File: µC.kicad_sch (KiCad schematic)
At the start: 18 parts, among them J1 Conn_01x02_Pin, J4 USB_C_Receptacle_USB2.0_14P, Q1 NPN, Q2 NPN, Q3 NPN, SW4 SW_Push, U2 ESP32-S3-WROOM-1

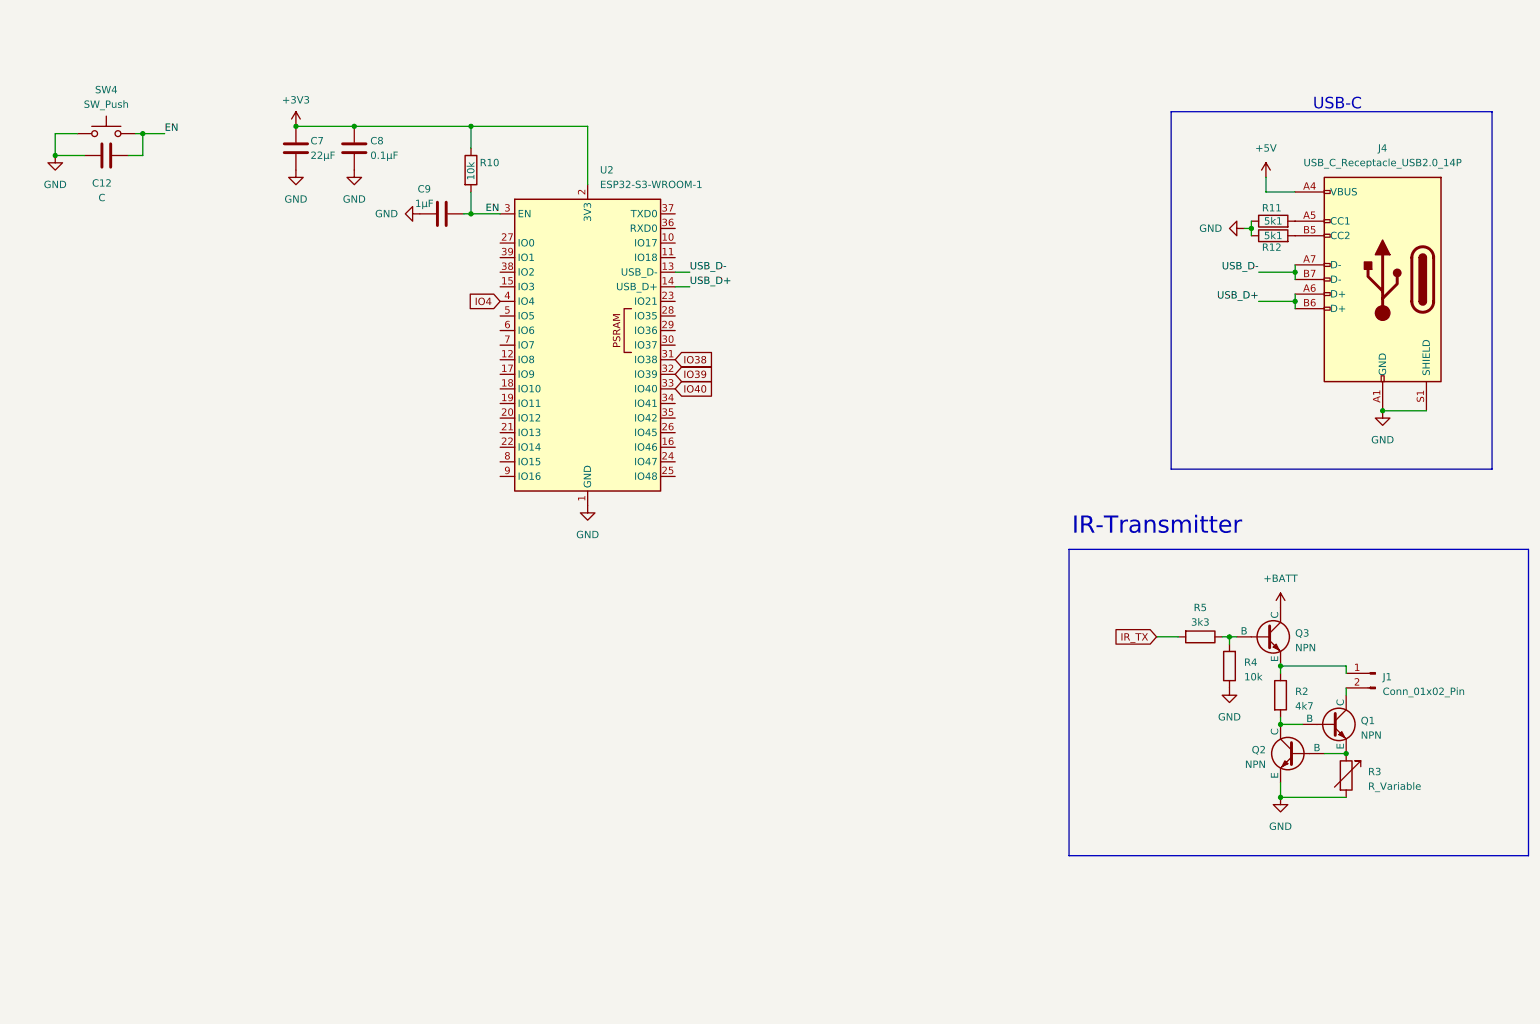
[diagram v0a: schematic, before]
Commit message: simulated IR-constant-current circuit, worked on schematic
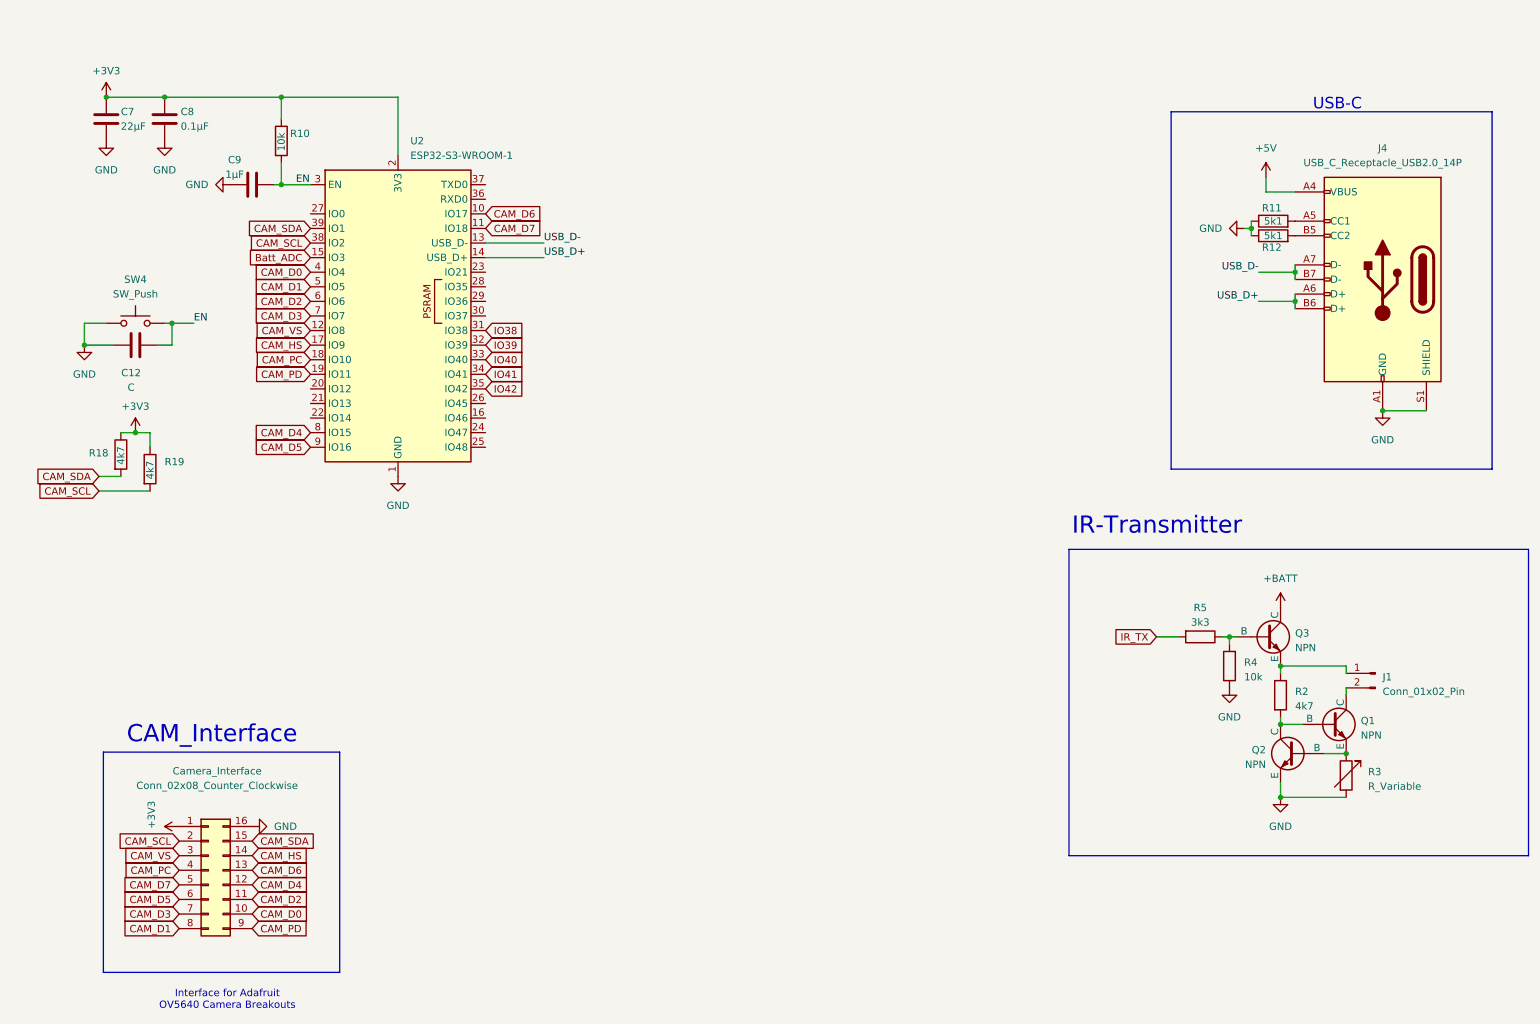
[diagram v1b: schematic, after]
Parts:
- added Camera_Interface: Conn_02x08_Counter_Clockwise, symbol Connector_Generic:Conn_02x08_Counter_Clockwise
- added R18, R19: 4k7, symbol Device:R
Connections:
- net +3V3: now also Camera_Interface.1 (Pin_1), R18.1, R19.1
- net GND: now also Camera_Interface.16 (Pin_16)
- net CAM_D6: now reaches U2.10 (IO17)
- net CAM_D6: now also Camera_Interface.13 (Pin_13)
- net CAM_D7: now reaches U2.11 (IO18)
- net CAM_D7: now also Camera_Interface.5 (Pin_5)
- net CAM_VS: now reaches U2.12 (IO8)
- net CAM_VS: now also Camera_Interface.3 (Pin_3)
- net Batt_ADC: now reaches U2.15 (IO3)
- net CAM_HS: now reaches U2.17 (IO9)
- net CAM_HS: now also Camera_Interface.14 (Pin_14)
- net CAM_PC: now reaches U2.18 (IO10)
- net CAM_PC: now also Camera_Interface.4 (Pin_4)
- net CAM_PD: now reaches U2.19 (IO11)
- net CAM_PD: now also Camera_Interface.9 (Pin_9)
- net IO41: now reaches U2.34 (IO41)
- net IO42: now reaches U2.35 (IO42)
- net CAM_SCL: now reaches U2.38 (IO2)
- net CAM_SCL: now also Camera_Interface.2 (Pin_2), R19.2
- net CAM_SDA: now reaches U2.39 (IO1)
- net CAM_SDA: now also Camera_Interface.15 (Pin_15), R18.2
- net CAM_D1: now reaches U2.5 (IO5)
- net CAM_D1: now also Camera_Interface.8 (Pin_8)
- net CAM_D2: now reaches U2.6 (IO6)
- net CAM_D2: now also Camera_Interface.11 (Pin_11)
- net CAM_D3: now reaches U2.7 (IO7)
- net CAM_D3: now also Camera_Interface.7 (Pin_7)
- net CAM_D4: now reaches U2.8 (IO15)
- net CAM_D4: now also Camera_Interface.12 (Pin_12)
- net CAM_D5: now reaches U2.9 (IO16)
- net CAM_D5: now also Camera_Interface.6 (Pin_6)
- net IO4 renamed CAM_D0
- net CAM_D0: now also Camera_Interface.10 (Pin_10)
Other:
- note added: "CAM_Interface"
- note added: "Interface for Adafruit OV5640 Camera Breakouts"
- moved on the sheet: C12, C7, C8, C9, R10, SW4, U2

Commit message: prepared for jlcpcb ordering.
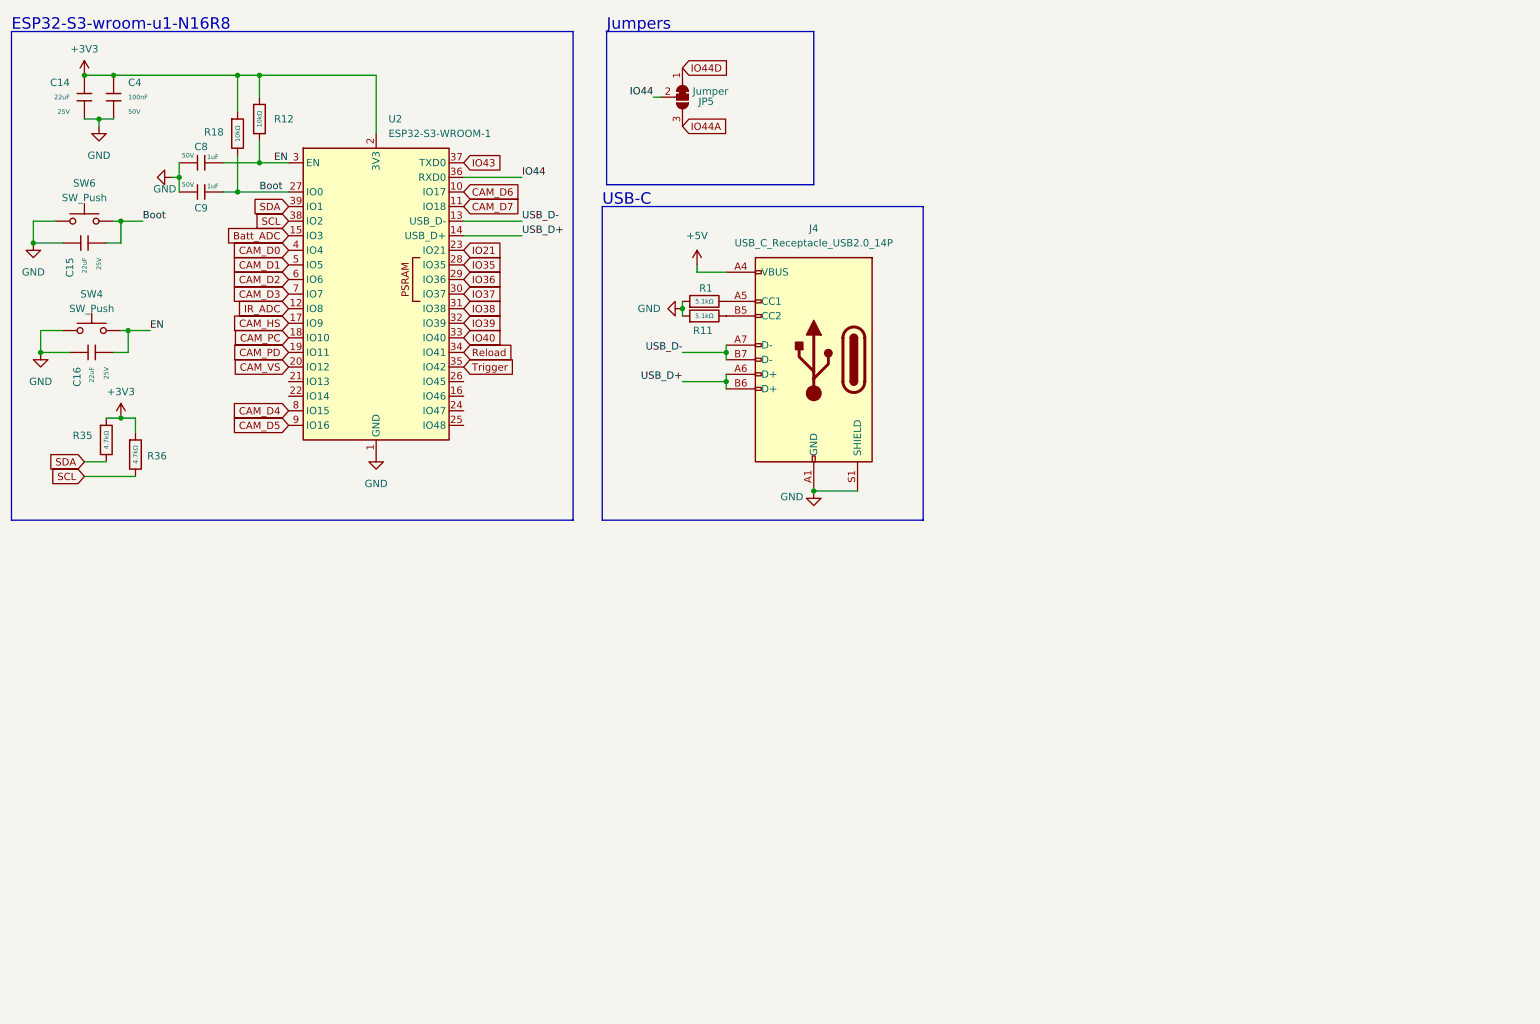
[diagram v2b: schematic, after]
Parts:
- removed C12: C, symbol Device:C
- removed C7: 22µF, symbol Device:C
- removed C8: 0.1µF, symbol Device:C
- removed C9: 1µF, symbol Device:C
- removed Camera_Interface: Conn_02x08_Counter_Clockwise, symbol Connector_Generic:Conn_02x08_Counter_Clockwise
- removed J1: Conn_01x02_Pin, symbol Connector:Conn_01x02_Pin
- removed Q1, Q2, Q3: NPN, symbol Simulation_SPICE:NPN
- removed R10, R4: 10k, symbol Device:R
- removed R11, R12: 5k1, symbol Device:R
- removed R18, R19, R2: 4k7, symbol Device:R
- removed R3: R_Variable, symbol Device:R_Variable
- removed R5: 3k3, symbol Device:R
- added C14, C15, C16: 22uF, PCM_JLCPCB:C_0805, symbol PCM_JLCPCB-Capacitors:0805,22uF
- added C4: 100nF, PCM_JLCPCB:C_0603, symbol PCM_JLCPCB-Capacitors:0603,100nF
- added C8, C9: 1uF, PCM_JLCPCB:C_0603, symbol PCM_JLCPCB-Capacitors:0603,1uF
- added JP5: Jumper, symbol Jumper:SolderJumper_3_Bridged12
- added R1, R11: 5.1kΩ, PCM_JLCPCB:R_0603, symbol PCM_JLCPCB-Resistors:0603,5.1kΩ
- added R12, R18: 10kΩ, PCM_JLCPCB:R_0603, symbol PCM_JLCPCB-Resistors:0603,10kΩ
- added R35, R36: 4.7kΩ, PCM_JLCPCB:R_0603, symbol PCM_JLCPCB-Resistors:0603,4.7kΩ
- added SW6: SW_Push, symbol Switch:SW_Push
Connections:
- net +3V3: now also C14.1, C4.1, R12.1, R18.1, R35.1, R36.1
- net CAM_VS: now also U2.20 (IO12); no longer U2.12 (IO8)
- net EN: now also C16.2, C8.2, R12.2
- net GND: now also C14.2, C15.1, C16.1, C4.2, C8.1, C9.1, R1.1, R11.1, SW6.1
- net IO21: now reaches U2.23 (IO21)
- net Boot: now reaches U2.27 (IO0)
- net Boot: now also C15.2, C9.2, R18.2, SW6.2
- net IO35: now reaches U2.28 (IO35)
- net IO36: now reaches U2.29 (IO36)
- net IO37: now reaches U2.30 (IO37)
- net IO44: now reaches U2.36 (RXD0)
- net IO44: now also JP5.2 (C)
- net IO43: now reaches U2.37 (TXD0)
- net at J4.B5 (CC2): now also R11.2
- net at J4.A5 (CC1): now also R1.2
- net CAM_SCL renamed SCL
- net SCL: now also R36.2
- net CAM_SDA renamed SDA
- net SDA: now also R35.2
- net IO41 renamed Reload
- net IO42 renamed Trigger
- new net IO44A: JP5.3 (B)
- new net IO44D: JP5.1 (A)
- new net IR_ADC: U2.12 (IO8)
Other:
- note added: "ESP32-S3-wroom-u1-N16R8"
- note added: "Jumpers"
- note removed: "CAM_Interface"
- note removed: "IR-Transmitter"
- note removed: "Interface for Adafruit OV5640 Camera Breakouts"
- moved on the sheet: J4, SW4, U2

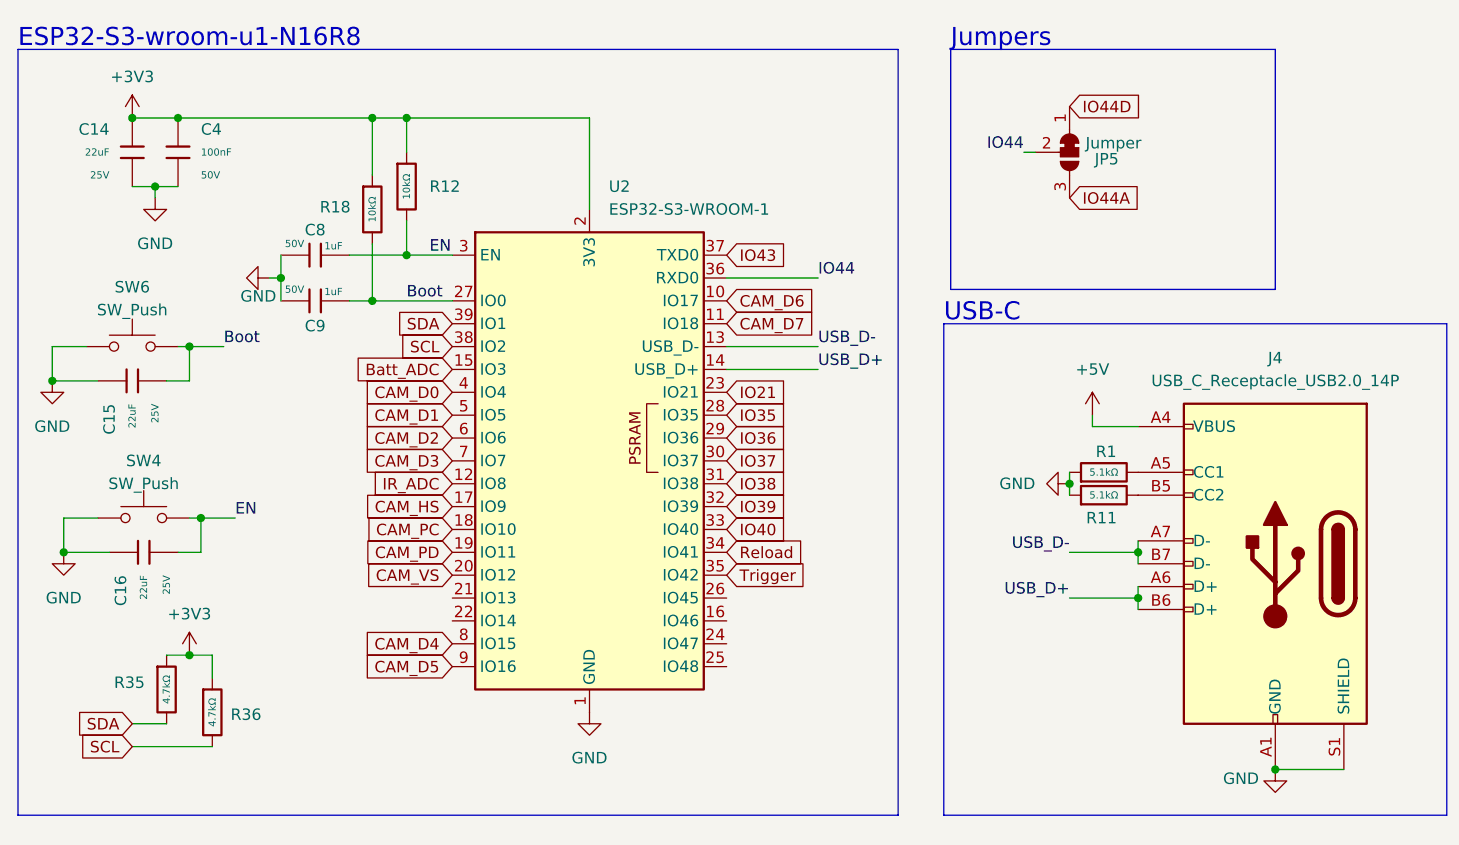
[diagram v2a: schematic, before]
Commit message: checked and fixed schematic, analized it with traceformer.io ai
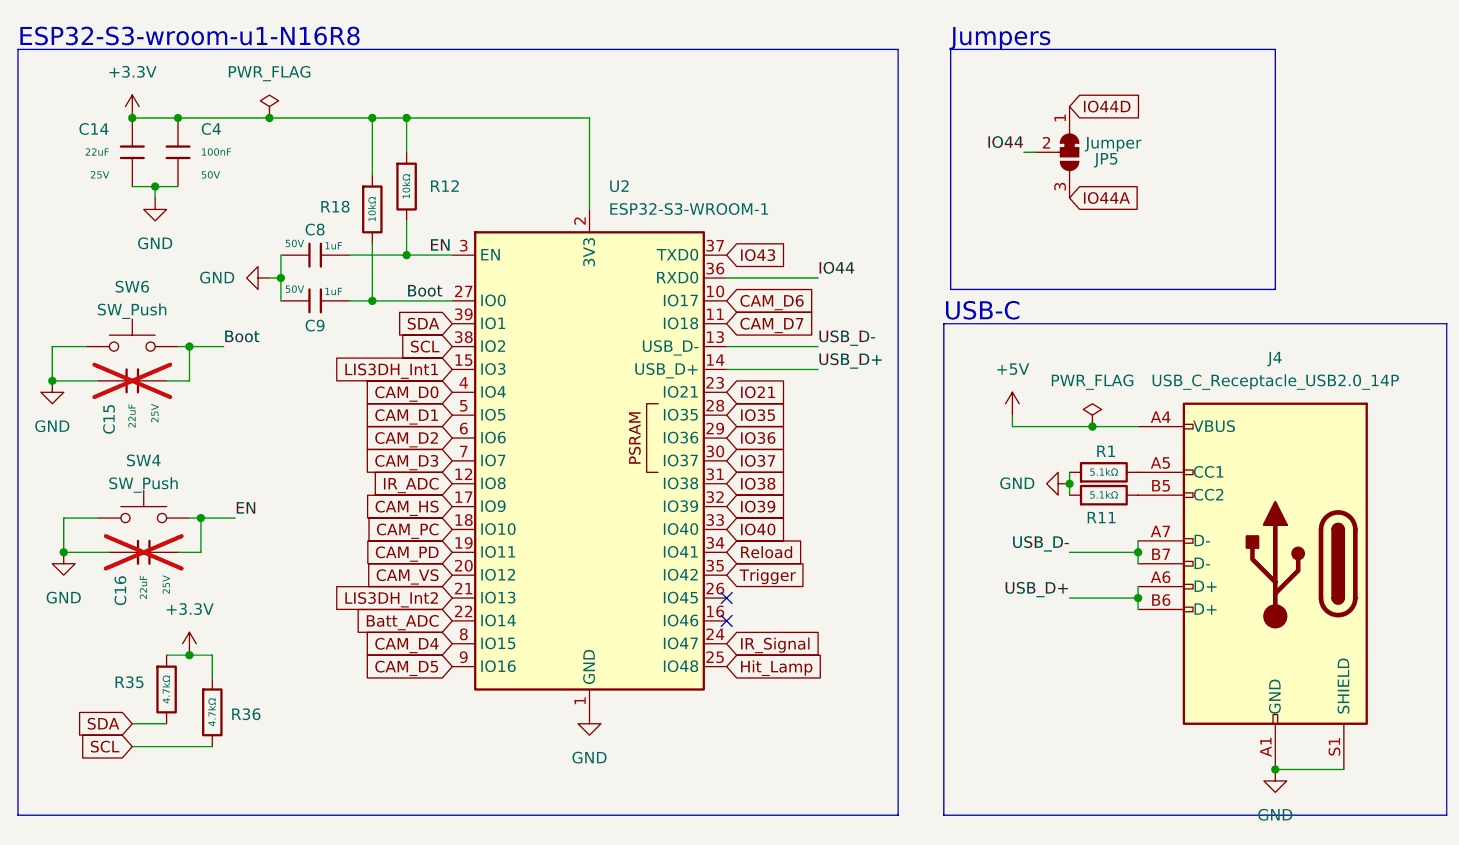
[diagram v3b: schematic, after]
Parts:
- C15, C16: now not fitted
- JP5: footprint (none) -> Jumper:SolderJumper-3_P1.3mm_Bridged12_RoundedPad1.0x1.5mm_NumberLabels
- SW4, SW6: footprint (none) -> Button_Switch_SMD:SW_SPST_CK_RS282G05A3
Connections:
- net Batt_ADC: now also U2.22 (IO14); no longer U2.15 (IO3)
- net LIS3DH_Int2: now reaches U2.21 (IO13)
- net IR_Signal: now reaches U2.24 (IO47)
- net Hit_Lamp: now reaches U2.25 (IO48)
- net +3V3 renamed +3.3V
- new net LIS3DH_Int1: U2.15 (IO3)
- no-connect marks 0 -> 2
